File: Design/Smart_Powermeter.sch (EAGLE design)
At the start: 48 parts, among them J1 AUDIO_JACK_TRRSSMD_RA, J2 AUDIO_JACK_TRRSSMD_RA, J3 AUDIO_JACK_TRRSSMD_RA, J4 AUDIO_JACK_TRRSSMD_RA, J5 AUDIO_JACK_TRRSSMD_RA, J6 AUDIO_JACK_TRRSSMD_RA, J7 AUDIO_JACK_TRRSSMD_RA, J8 AUDIO_JACK_TRRSSMD_RA

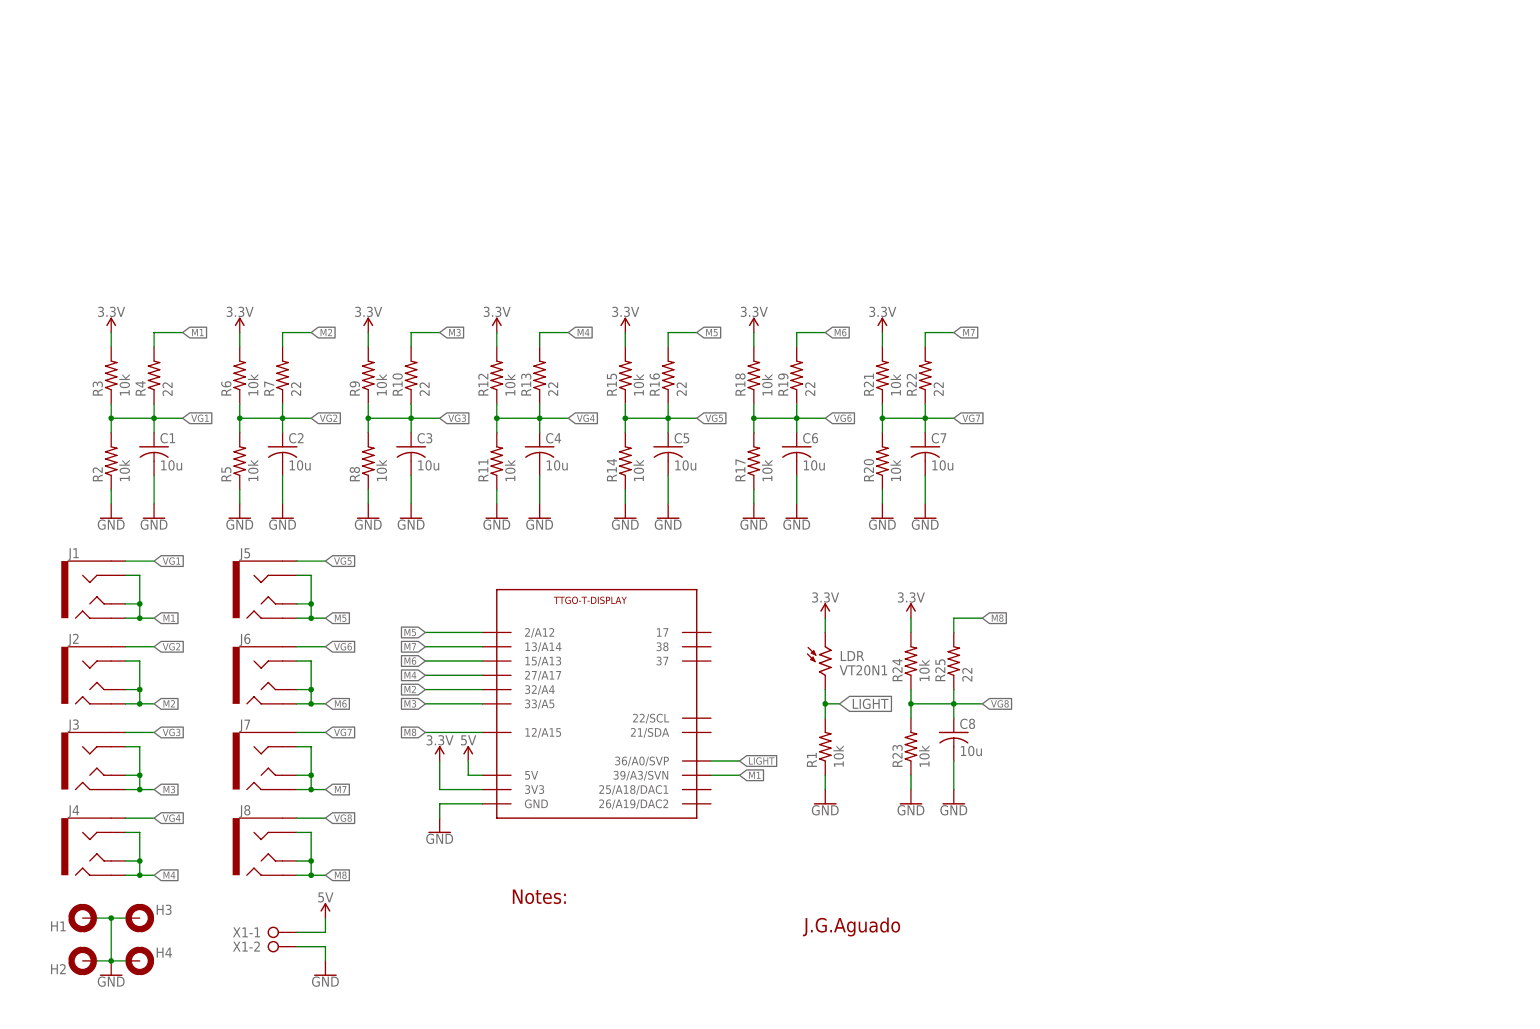
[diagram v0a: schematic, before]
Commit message: Updated design files fixing Release 1 bugs
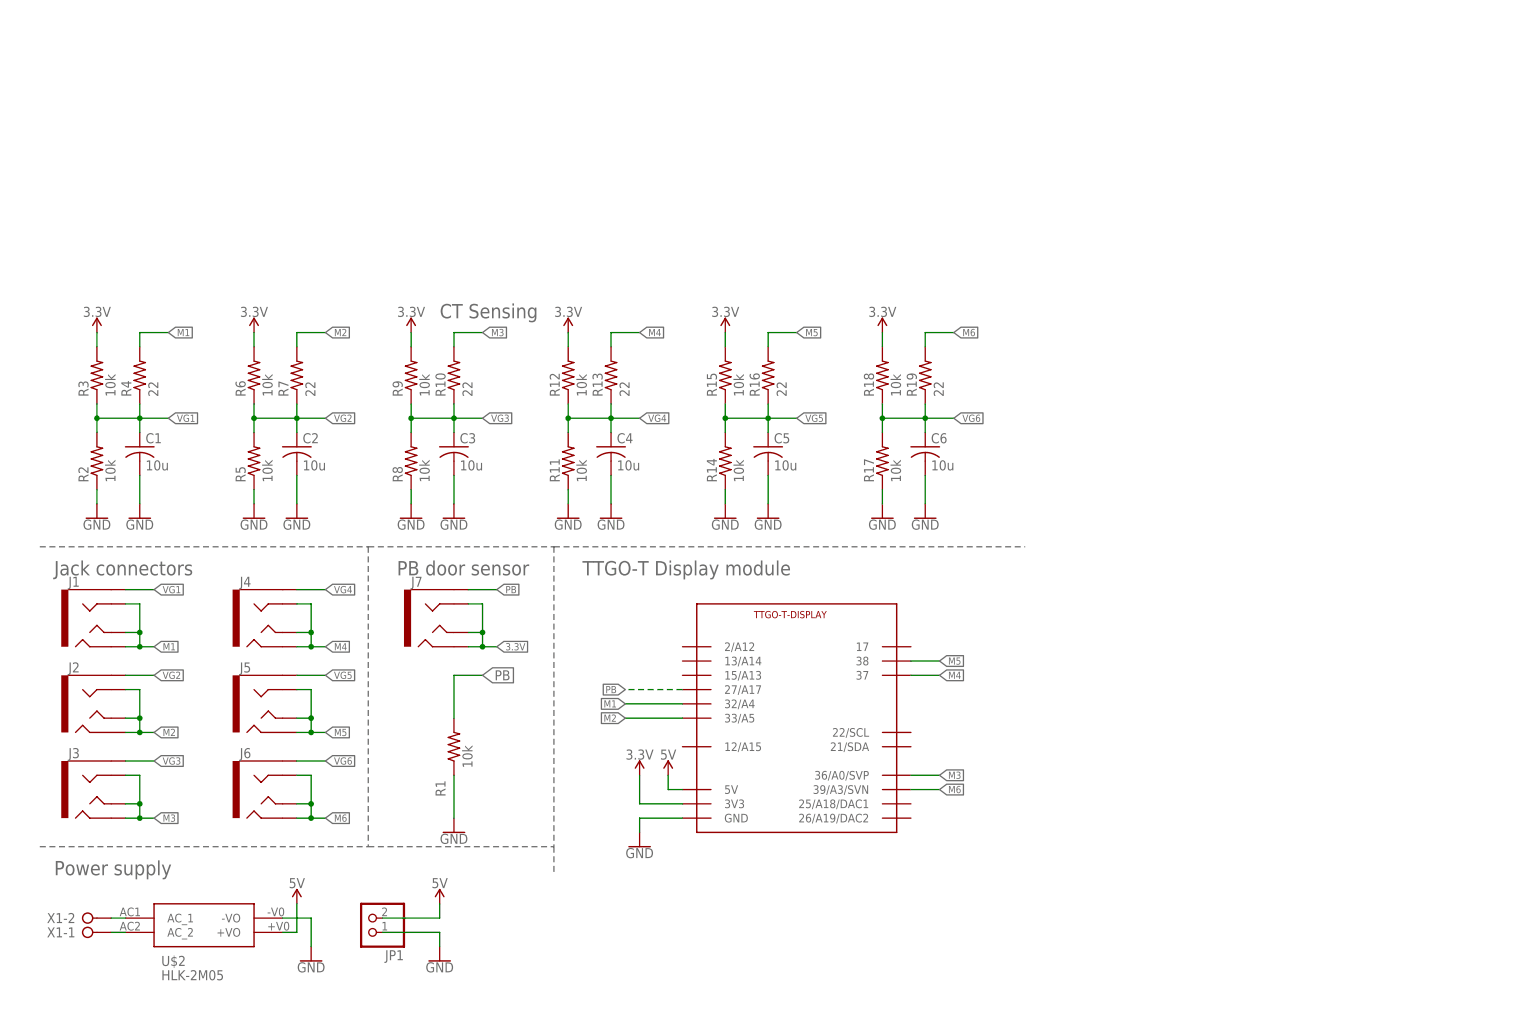
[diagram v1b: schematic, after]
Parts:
- removed C7, C8: 10u, rcl:C-USC0603
- removed H1, H2, H3, H4: MOUNT-PAD-ROUND3.0, holes:MOUNT-PAD-ROUND3.0
- removed J8: AUDIO_JACK_TRRSSMD_RA, SparkFun-Connectors:AUDIO_JACK_TRRSSMD_RA
- removed LDR: VT20N1, photo-elements:VT20N1
- removed R20, R21, R23, R24: 10k, rcl:R-US_R0603
- removed R22, R25: 22, rcl:R-US_R1206
- added JP1: (no value), pinhead:PINHD-1X2
- added U$2: HLK-2M05, SpaceDIY_modules:HLK-2M05
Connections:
- removed net LIGHT: LDR.2, R1.2, U$1.36/A0/SVP
- removed net M7: J7.RING1, J7.RING2, J7.TIP, R22.2, U$1.13/A14
- removed net M8: J8.RING1, J8.RING2, J8.TIP, R25.2, U$1.12/A15
- removed net VG7: C7.1, J7.EARTH, R20.2, R21.1, R22.1
- removed net VG8: C8.1, J8.EARTH, R23.2, R24.1, R25.1
- new net N$1: U$2.AC_1, X1-2.KL
- new net N$2: U$2.AC_2, X1-1.KL
- new net PB: J7.EARTH, R1.2, U$1.27/A17
- net 3.3V: now also J7.RING1, J7.RING2, J7.TIP; no longer LDR.1, R21.2, R24.2
- net 5V: now also JP1.2, U$2.+VO; no longer X1-1.KL
- net GND: now also JP1.1, U$2.-VO; no longer C7.2, C8.2, H1.MOUNT, H2.MOUNT, H3.MOUNT, H4.MOUNT, R20.1, R23.1, X1-2.KL
- net M1: now also U$1.32/A4; no longer U$1.39/A3/SVN
- net M2: now also U$1.33/A5; no longer U$1.32/A4
- net M3: now also U$1.36/A0/SVP; no longer U$1.33/A5
- net M4: now also U$1.37; no longer U$1.27/A17
- net M5: now also U$1.38; no longer U$1.2/A12
- net M6: now also U$1.39/A3/SVN; no longer U$1.15/A13
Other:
- note added: "CT Sensing"
- note added: "Jack connectors"
- note added: "PB door sensor"
- note added: "Power supply"
- note added: "TTGO-T Display module"
- note removed: "J.G.Aguado"
- note removed: "Notes:"
- moved on the sheet: C1, C2, C3, C4, C5, C6, J1, J2, J3, J4, J5, J6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

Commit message: Resize dimensions to fit in the 92x87 enclosure
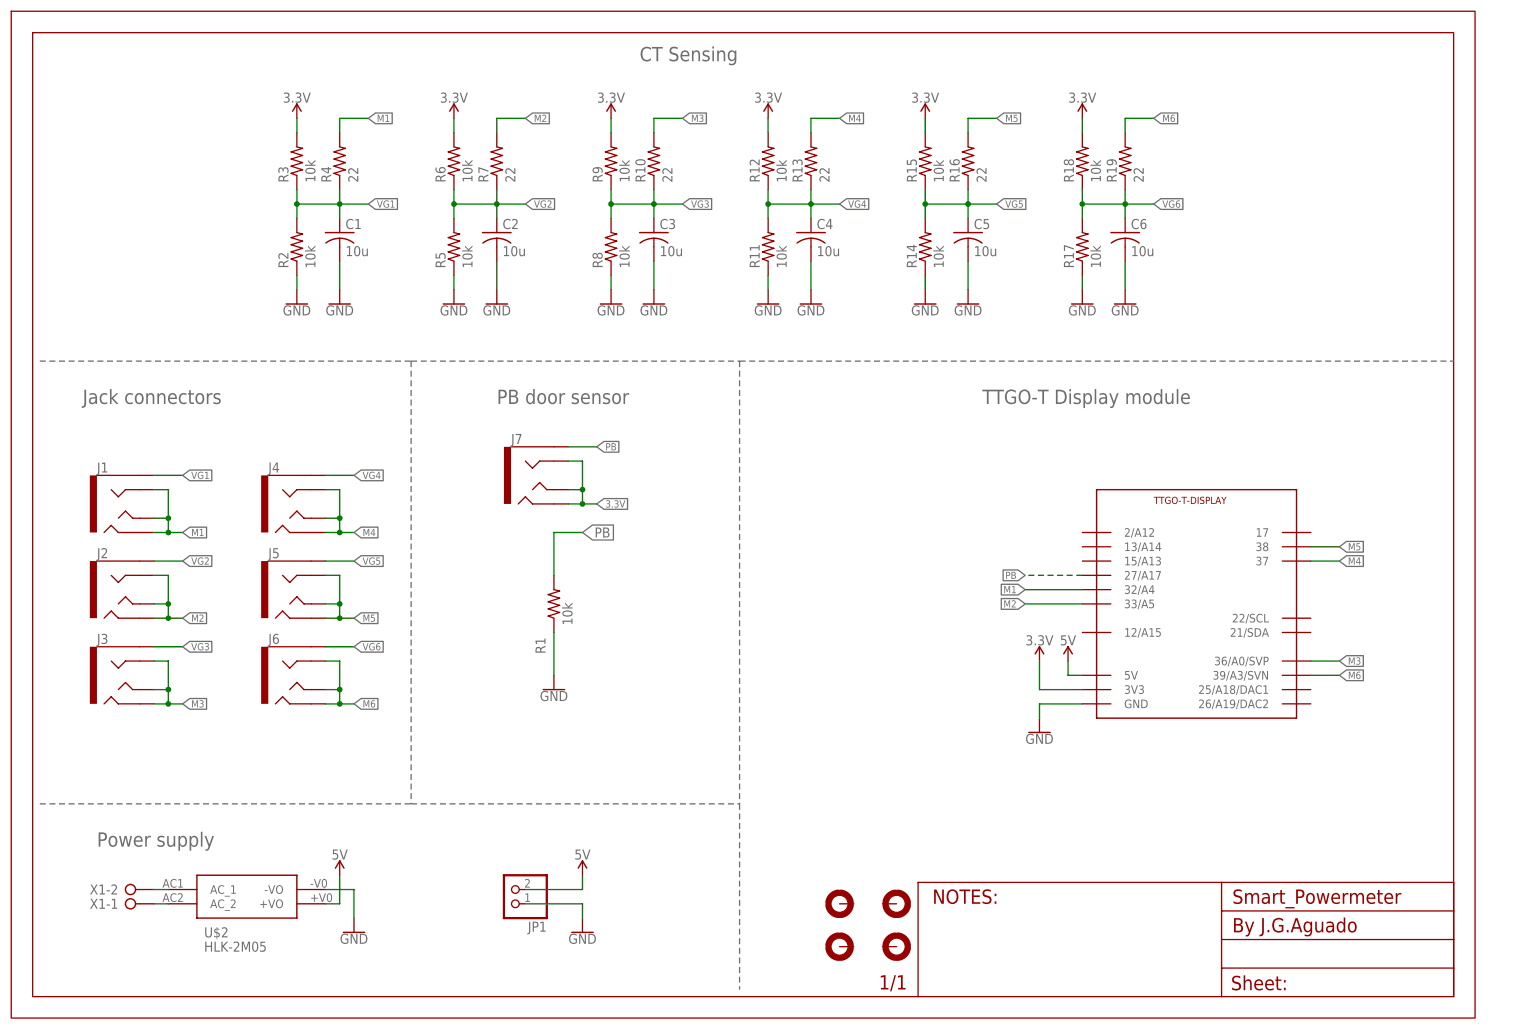
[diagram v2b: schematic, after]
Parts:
- added FRAME1: (no value), SpaceDIY_symbols:A4L-LOC
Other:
- moved on the sheet: C1, C2, C3, C4, C5, C6, J1, J2, J3, J4, J5, J6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

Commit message: Added design files of V2
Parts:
- removed FRAME1: (no value), SpaceDIY_symbols:A4L-LOC
- removed JP1: (no value), pinhead:PINHD-1X2
- added C10, C12, C16, C20, C8: 10uF, rcl:C-USC0603
- added C11, C15, C21: 0.1uF, rcl:C-USC0603
- added C13, C14, C17, C18, C19, C25, C27, C28, C9: 1uF, rcl:C-USC0603
- added C26, C7: 4.7uF, rcl:C-USC0603
- added D1, D2, D3: SS14, SpaceDIY_semiconductors:DIODE-SCHOTTKYSS14
- added DISP1: DISP_LCD_GENERIC_SPI_1.69_WRAPUNDER, adafruit_display:DISP_LCD_GENERIC_SPI_1.69_WRAPUNDER
- added H1: 92X84, SpaceDIY_symbols:92X84
- added IC1: AMS1117-3.3, SparkFun-IC-Power:V_REG_LD1117VXXLD1117-SMD
- added IC3: ESP32-S2-MINI-1-N4R2, SpaceDIY_modules:ESP32-S2-MINI-1-N4R2
- added IC5: BMP280, SamacSys_Parts:BMP280
- added J8: USB-C, SparkFun-Connectors:USB_C_4-LAYER-ISOLATED
- added L3: 10uH, microbuilder:INDUCTORNR401
- added Q1: IRLML0100, Parts:IRLML2060TRPBF
- added Q2: 2N7002, SparkFun-DiscreteSemi:MOSFET-NCH-BSS138
- added R20, R21, R22, R26, R28, R29: 10k, rcl:R-US_R0603
- added R23, R24: 4.7k, rcl:R-US_R0603
- added R25: 10K, rcl:R-US_R0603
- added R27: 10, rcl:R-US_R0603
- added R36, R37: 5.1k, rcl:R-US_R0603
- added S1: Flash, SpaceDIY_electromechanical:MOMENTARY-SWITCH-SPST-SMD-5.2MM-TALL
- added S2: Reset, SpaceDIY_electromechanical:MOMENTARY-SWITCH-SPST-SMD-5.2MM-TALL
- added SJ1, SJ2: SOLDERJUMPERROUND, SparkFun-Retired:SOLDERJUMPERROUND
- J7: value AUDIO_JACK_TRRSSMD_RA -> (none); device SparkFun-Connectors:AUDIO_JACK_TRRSSMD_RA -> SparkFun-Connectors:CONN_04PTH
- R1: value 10k -> 0.47
- U$1: value TTGO-T-DISPLAYFRAME -> E-PAPER-FPC_2; device TTGO-TDisplay:TTGO-T-DISPLAYFRAME -> SpaceDIY_connectors:E-PAPER-FPC_2
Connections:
- removed net M6: J6.RING1, J6.RING2, J6.TIP, R19.2, U$1.39/A3/SVN
- removed net PB: J7.EARTH, R1.2, U$1.27/A17
- removed net VG6: C6.1, J6.EARTH, R17.2, R18.1, R19.1
- new net BK_LIGHT: Q2.G, R26.1
- new net CC3: J8.CC2, R36.2
- new net CC4: J8.CC1, R37.2
- new net D+: IC3.IO20, J8.D+
- new net D-: IC3.IO19, J8.D-
- new net GDR: Q1.G, R20.1, U$1.2
- new net IO0: IC3.IO0, S1.2
- new net LEDK: DISP1.LEDK, R27.2
- new net M0: IC3.IO1, J1.RING1, J1.RING2, J1.TIP, R4.2
- new net N$10: IC5.SDO, R23.2
- new net N$11: C9.2, U$1.5
- new net N$12: C13.2, U$1.18
- new net N$13: C14.2, U$1.20
- new net N$14: C17.2, U$1.22
- new net N$15: C18.2, U$1.24
- new net N$16: C26.2, D2.A, D3.C
- new net N$17: C26.1, D1.A, L3.1, Q1.D
- new net N$3: IC5.CSB, R24.2
- new net N$31: C27.2, U$1.4
- new net N$32: C28.2, U$1.19
- new net N$4: Q2.D, R27.1
- new net N$5: R28.1, SJ1.2
- new net N$6: R29.1, SJ2.2
- new net RESE: Q1.S, R1.1, U$1.3
- new net RST: IC3.EN, R25.1, S2.2
- new net RX: IC3.RXD0, J7.4
- new net SCL: IC3.IO34, IC5.SCK, R21.2
- new net SDA: IC3.IO33, IC5.SDI, R22.2
- new net SPI_BUSY: IC3.IO14, U$1.9
- new net SPI_CLK: DISP1.CLOCK, IC3.IO12, U$1.13
- new net SPI_CS: DISP1.CS, IC3.IO10, SJ2.1, U$1.12
- new net SPI_MISO: DISP1.RS/DC, IC3.IO13, U$1.11
- new net SPI_MOSI: DISP1.DATA, IC3.IO11, U$1.14
- new net SPI_RST: DISP1.RESET, IC3.IO15, SJ1.1, U$1.10
- new net TX: IC3.TXD0, J7.3
- new net VG0: C1.1, J1.EARTH, R2.2, R3.1, R4.1
- new net VGH: C19.1, D1.C, U$1.21
- new net VGL: C25.1, D3.A, U$1.23
- net 3.3V: now also C10.1, C11.1, C12.1, C15.1, C16.1, C20.1, C21.1, C7.1, DISP1.LEDA, DISP1.VDD, IC1.OUT, IC3.3V3, IC5.VDDIO_1, IC5.VDDIO_2, L3.2, R21.1, R22.1, R23.1, R24.1, R25.2, R26.2, R28.2, R29.2, U$1.15, U$1.16; no longer J7.RING1, J7.RING2, J7.TIP, U$1.3V3
- net 5V: now also C8.1, IC1.IN, J7.1, J8.VBUS; no longer JP1.2, U$1.5V
- net GND: now also C10.2, C11.2, C12.2, C13.1, C14.1, C15.2, C16.2, C17.1, C18.1, C19.2, C20.2, C21.2, C25.2, C27.1, C28.1, C7.2, C8.2, C9.1, D2.C, DISP1.GND, H1.MOUNT, IC1.GND, IC3.GND_1, IC3.GND_10, IC3.GND_11, IC3.GND_12, IC3.GND_13, IC3.GND_14, IC3.GND_15, IC3.GND_16, IC3.GND_17, IC3.GND_18, IC3.GND_19, IC3.GND_2, IC3.GND_20, IC3.GND_21, IC3.GND_22, IC3.GND_23, IC3.GND_24, IC3.GND_25, IC3.GND_26, IC3.GND_27, IC3.GND_28, IC3.GND_29, IC3.GND_3, IC3.GND_30, IC3.GND_31, IC3.GND_32, IC3.GND_33, IC3.GND_4, IC3.GND_5, IC3.GND_6, IC3.GND_7, IC3.GND_8, IC3.GND_9, IC5.GND_1, IC5.GND_2, J7.2, J8.GND, Q2.S, R1.2, R20.2, R36.1, R37.1, S1.1, S2.1, U$1.17, U$1.8; no longer JP1.1, R1.1, U$1.GND
- net M1: now also IC3.IO2, J2.RING1, J2.RING2, J2.TIP, R7.2; no longer J1.RING1, J1.RING2, J1.TIP, R4.2, U$1.32/A4
- net M2: now also IC3.IO3, J3.RING1, J3.RING2, J3.TIP, R10.2; no longer J2.RING1, J2.RING2, J2.TIP, R7.2, U$1.33/A5
- net M3: now also IC3.IO4, J4.RING1, J4.RING2, J4.TIP, R13.2; no longer J3.RING1, J3.RING2, J3.TIP, R10.2, U$1.36/A0/SVP
- net M4: now also IC3.IO5, J5.RING1, J5.RING2, J5.TIP, R16.2; no longer J4.RING1, J4.RING2, J4.TIP, R13.2, U$1.37
- net M5: now also IC3.IO6, J6.RING1, J6.RING2, J6.TIP, R19.2; no longer J5.RING1, J5.RING2, J5.TIP, R16.2, U$1.38
- net N$1: now also U$2.AC_2; no longer U$2.AC_1
- net N$2: now also U$2.AC_1; no longer U$2.AC_2
- net VG1: now also C2.1, J2.EARTH, R5.2, R6.1, R7.1; no longer C1.1, J1.EARTH, R2.2, R3.1, R4.1
- net VG2: now also C3.1, J3.EARTH, R10.1, R8.2, R9.1; no longer C2.1, J2.EARTH, R5.2, R6.1, R7.1
- net VG3: now also C4.1, J4.EARTH, R11.2, R12.1, R13.1; no longer C3.1, J3.EARTH, R10.1, R8.2, R9.1
- net VG4: now also C5.1, J5.EARTH, R14.2, R15.1, R16.1; no longer C4.1, J4.EARTH, R11.2, R12.1, R13.1
- net VG5: now also C6.1, J6.EARTH, R17.2, R18.1, R19.1; no longer C5.1, J5.EARTH, R14.2, R15.1, R16.1
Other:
- note added: "230V power supply"
- note added: "Microcontroller"
- note added: "Power reg"
- note added: "Reset & Flash switches"
- note added: "Serial port"
- note added: "TFT Display"
- note added: "Temperature & humidity sensor"
- note added: "USB-C"
- note added: "eInk Display"
- note removed: "PB door sensor"
- note removed: "Power supply"
- note removed: "TTGO-T Display module"

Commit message: Updated design files
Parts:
- removed C15, C21: 0.1uF, rcl:C-USC0603
- removed C16, C20: 10uF, rcl:C-USC0603
- removed DISP1: DISP_LCD_GENERIC_SPI_1.69_WRAPUNDER, adafruit_display:DISP_LCD_GENERIC_SPI_1.69_WRAPUNDER
- removed IC5: BMP280, SamacSys_Parts:BMP280
- removed Q2: 2N7002, SparkFun-DiscreteSemi:MOSFET-NCH-BSS138
- removed R21, R22, R26, R28, R29: 10k, rcl:R-US_R0603
- removed R23, R24: 4.7k, rcl:R-US_R0603
- removed R27: 10, rcl:R-US_R0603
- removed SJ1, SJ2: SOLDERJUMPERROUND, SparkFun-Retired:SOLDERJUMPERROUND
- added J9: (no value), SparkFun-Connectors:CONN_04PTH
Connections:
- removed net BK_LIGHT: Q2.G, R26.1
- removed net LEDK: DISP1.LEDK, R27.2
- removed net M0: IC3.IO1, J1.RING1, J1.RING2, J1.TIP, R4.2
- removed net N$10: IC5.SDO, R23.2
- removed net N$3: IC5.CSB, R24.2
- removed net N$4: Q2.D, R27.1
- removed net N$5: R28.1, SJ1.2
- removed net N$6: R29.1, SJ2.2
- new net M6: IC3.IO6, J6.RING1, J6.RING2, J6.TIP, R19.2
- net 3.3V: now also J9.2; no longer C15.1, C16.1, C20.1, C21.1, DISP1.LEDA, DISP1.VDD, IC5.VDDIO_1, IC5.VDDIO_2, R21.1, R22.1, R23.1, R24.1, R26.2, R28.2, R29.2
- net GND: now also J9.1; no longer C15.2, C16.2, C20.2, C21.2, DISP1.GND, IC5.GND_1, IC5.GND_2, Q2.S
- net M1: now also IC3.IO1, J1.RING1, J1.RING2, J1.TIP, R4.2; no longer IC3.IO2, J2.RING1, J2.RING2, J2.TIP, R7.2
- net M2: now also IC3.IO2, J2.RING1, J2.RING2, J2.TIP, R7.2; no longer IC3.IO3, J3.RING1, J3.RING2, J3.TIP, R10.2
- net M3: now also IC3.IO3, J3.RING1, J3.RING2, J3.TIP, R10.2; no longer IC3.IO4, J4.RING1, J4.RING2, J4.TIP, R13.2
- net M4: now also IC3.IO4, J4.RING1, J4.RING2, J4.TIP, R13.2; no longer IC3.IO5, J5.RING1, J5.RING2, J5.TIP, R16.2
- net M5: now also IC3.IO5, J5.RING1, J5.RING2, J5.TIP, R16.2; no longer IC3.IO6, J6.RING1, J6.RING2, J6.TIP, R19.2
- net SCL: now also J9.4; no longer IC5.SCK, R21.2
- net SDA: now also J9.3; no longer IC5.SDI, R22.2
- net SPI_CLK: no longer DISP1.CLOCK
- net SPI_CS: no longer DISP1.CS, SJ2.1
- net SPI_MISO: no longer DISP1.RS/DC
- net SPI_MOSI: no longer DISP1.DATA
- net SPI_RST: no longer DISP1.RESET, SJ1.1
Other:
- note added: "IIC port"
- note removed: "TFT Display"
- note removed: "Temperature & humidity sensor"
- moved on the sheet: C10, C13, C14, C17, C18, C19, C25, C26, C27, C28, C7, C8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
